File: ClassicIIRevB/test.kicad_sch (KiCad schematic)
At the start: 93 parts

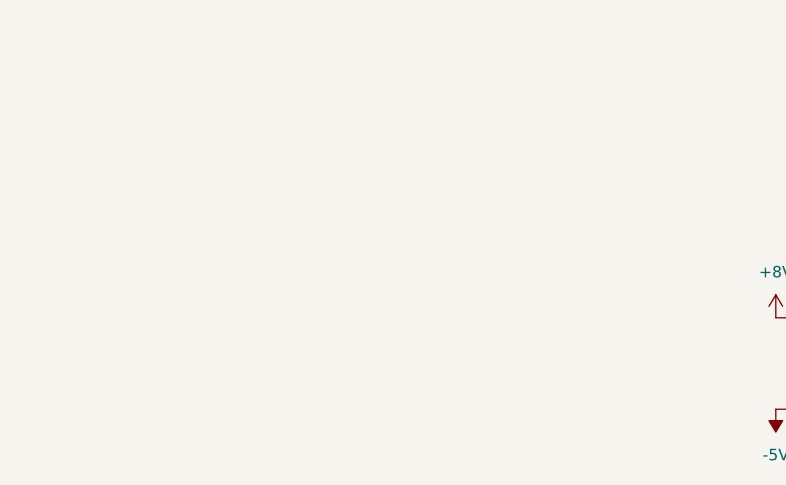
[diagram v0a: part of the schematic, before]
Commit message: Show smaller ROM footprints
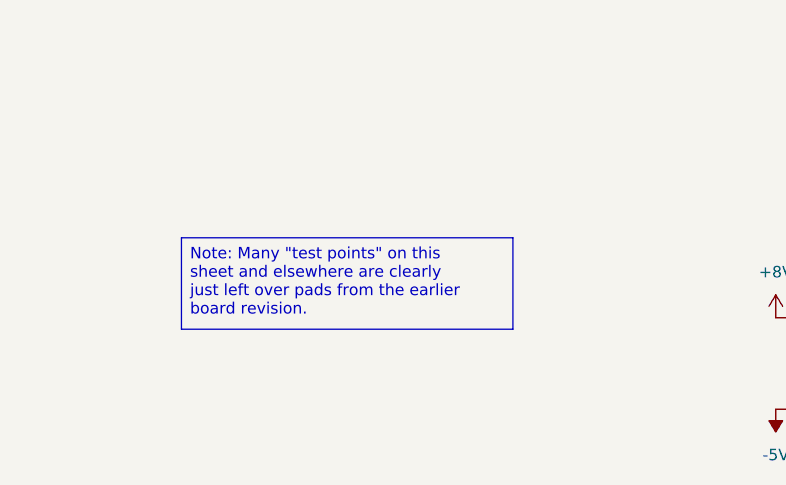
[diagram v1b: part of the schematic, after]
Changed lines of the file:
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@@
 	(title_block
 		(title "Macintosh Classic II Revision B")
-		(date "2025-05-29")
+		(date "2025-05-31")
 		(company "Apple Computer")
 		(comment 1 "drawn by Bradley Bell")
 	)
+	(text_box "Note: Many \"test points\" on this sheet and elsewhere are clearly just left over pads from the earlier board revision."
+		(exclude_from_sim no)
+		(at 48.26 171.45 0)
+		(size 36.83 10.16)
+		(margins 0.9525 0.9525 0.9525 0.9525)
+		(stroke
+			(width 0)
+			(type solid)
+		)
+		(fill
+			(type none)
+		)
+		(effects
+			(font
+				(size 1.27 1.27)
+			)
+			(justify left top)
+		)
+	)
 	(junction

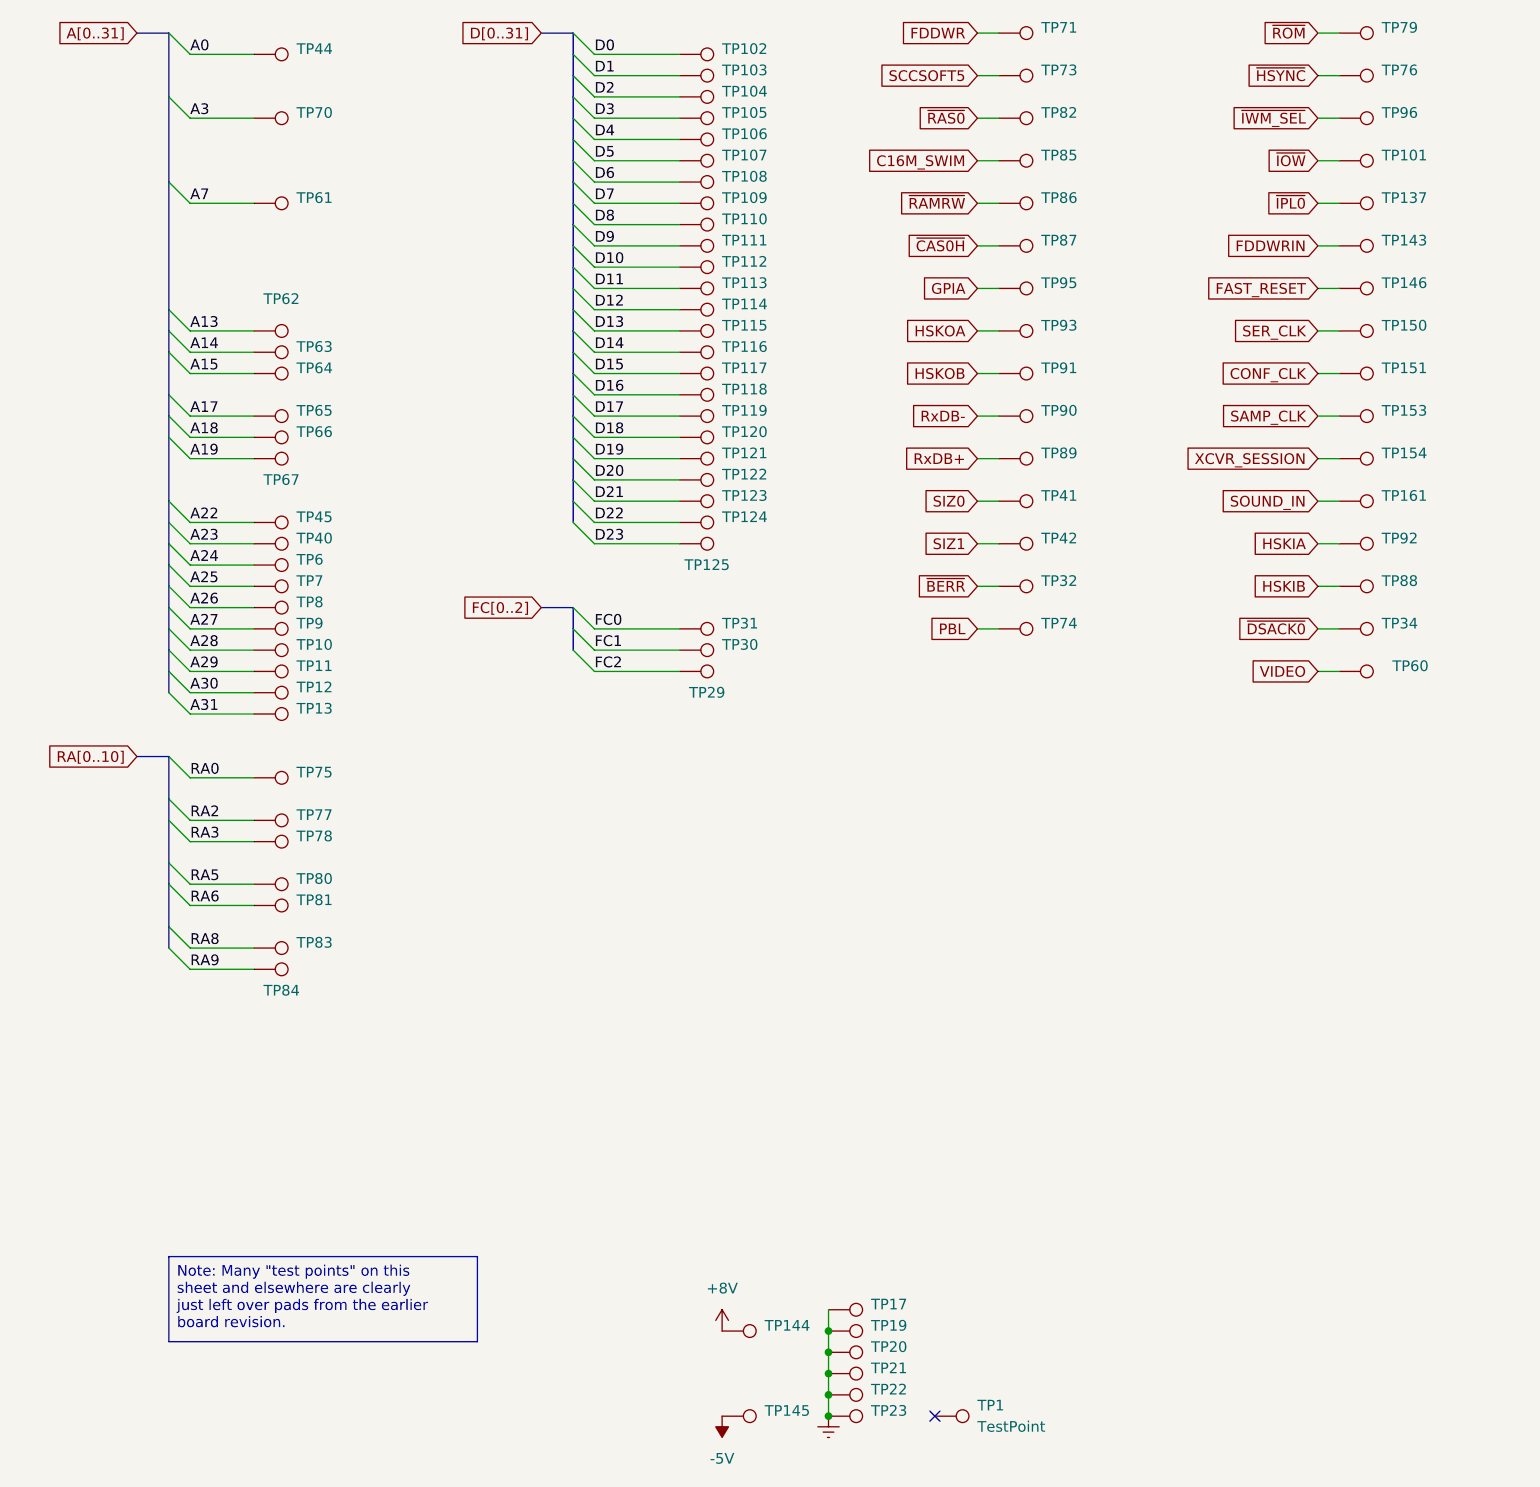
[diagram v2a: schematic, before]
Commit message: Switch to some "official" net names
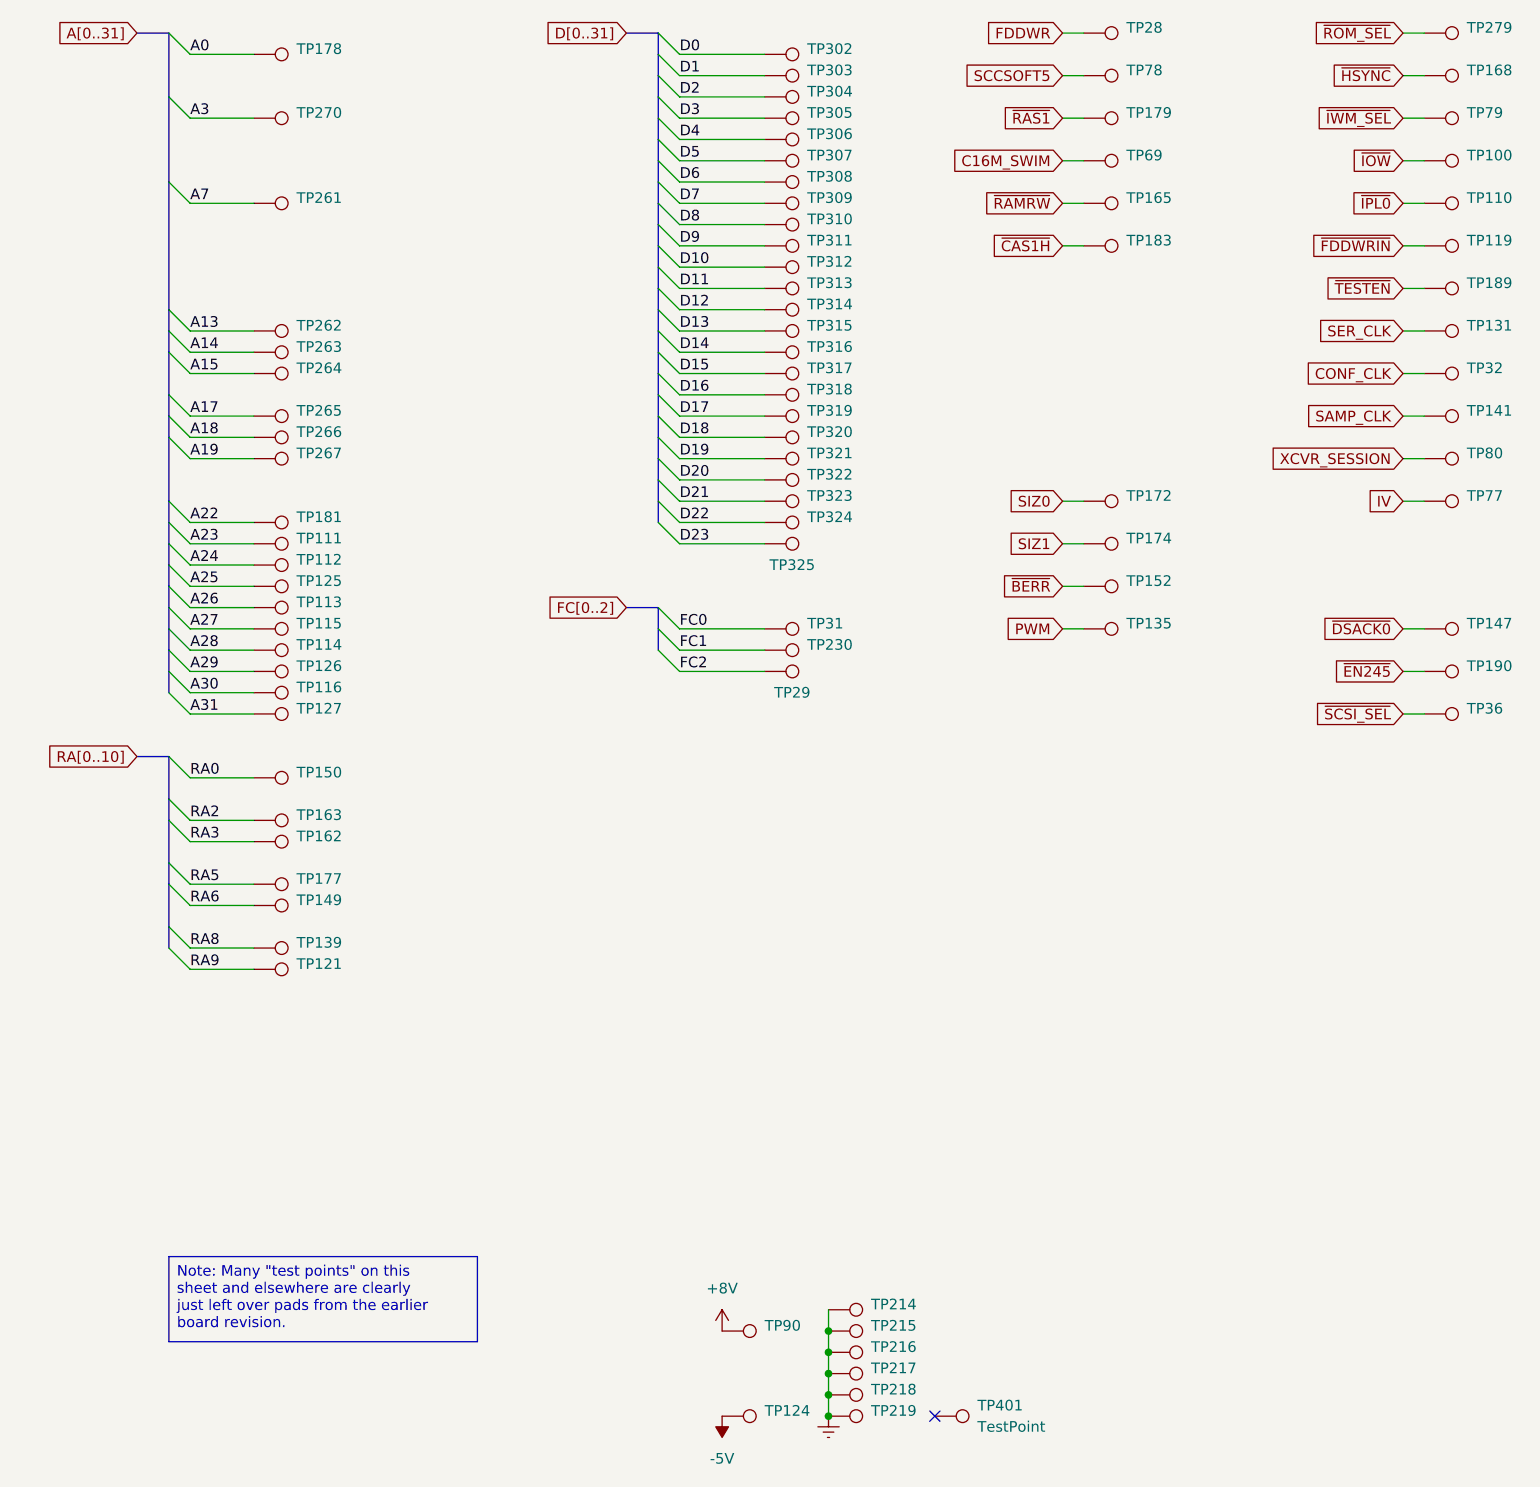
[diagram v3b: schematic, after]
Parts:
- removed TP60, TP88, TP89, TP90, TP92: ~, MyPackage:TestPoint_THTPad_D1.0mm_Drill0.5mm, symbol Connector:TestPoint
- removed TP91, TP93, TP95: ~, MyPackage:TestPoint_Pad_D1.0mm, symbol Connector:TestPoint
- added TP190, TP36: ~, MyPackage:TestPoint_THTPad_D1.0mm_Drill0.5mm, symbol Connector:TestPoint
- renumbered TP101 to TP100, TP137 to TP110, TP40 to TP111, TP6 to TP112, TP8 to TP113, TP10 to TP114, TP9 to TP115, TP12 to TP116, TP143 to TP119, TP84 to TP121, TP145 to TP124, TP7 to TP125, TP11 to TP126, TP13 to TP127, TP150 to TP131, TP74 to TP135, TP83 to TP139, TP153 to TP141, TP34 to TP147, TP81 to TP149, TP75 to TP150, TP32 to TP152, TP78 to TP162, TP77 to TP163, TP86 to TP165, TP76 to TP168, TP41 to TP172, TP42 to TP174, TP80 to TP177, TP44 to TP178, TP82 to TP179, TP45 to TP181, TP87 to TP183, TP146 to TP189, TP17 to TP214, TP19 to TP215, TP20 to TP216, TP21 to TP217, TP22 to TP218, TP23 to TP219, TP30 to TP230, TP61 to TP261, TP62 to TP262, TP63 to TP263, TP64 to TP264, TP65 to TP265, TP66 to TP266, TP67 to TP267, TP70 to TP270, TP79 to TP279, TP71 to TP28, TP102 to TP302, TP103 to TP303, TP104 to TP304, TP105 to TP305, TP106 to TP306, TP107 to TP307, TP108 to TP308, TP109 to TP309, TP110 to TP310, TP111 to TP311, TP112 to TP312, TP113 to TP313, TP114 to TP314, TP115 to TP315, TP116 to TP316, TP117 to TP317, TP118 to TP318, TP119 to TP319, TP151 to TP32, TP120 to TP320, TP121 to TP321, TP122 to TP322, TP123 to TP323, TP124 to TP324, TP125 to TP325, TP1 to TP401, TP85 to TP69, TP161 to TP77, TP73 to TP78, TP96 to TP79, TP154 to TP80, TP144 to TP90
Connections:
- net FAST_RESET renamed ~{TESTEN}
- net FDDWRIN renamed ~{FDDWRIN}
- net PBL renamed PWM
- net SOUND_IN renamed IV
- net ~{CAS0H} renamed ~{CAS1H}
- net ~{RAS0} renamed ~{RAS1}
- net ~{ROM} renamed ~{ROM_SEL}
- new net ~{EN245}: TP190.1
- new net ~{SCSI_SEL}: TP36.1
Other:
- moved on the sheet: TP100, TP110, TP119, TP131, TP135, TP141, TP147, TP152, TP165, TP168, TP172, TP174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

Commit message: update exports
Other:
- title: Macintosh Classic II Revision B -> Macintosh Classic II (Later Revision)
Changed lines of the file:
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@@
 	(paper "USLetter")
 	(title_block
-		(title "Macintosh Classic II Revision B")
-		(date "2025-06-04")
+		(title "Macintosh Classic II (Later Revision)")
+		(date "2025-06-16")
 		(company "Apple Computer")
 		(comment 1 "drawn by Bradley Bell")

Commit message: Corrections to SMDs, more improved footprints
The later revision board reproduction design is now complete.
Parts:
- TP100, TP110, TP111, TP112, TP113, TP114, TP115, TP116, TP119, TP121, TP124, TP125, TP126, TP127, TP131, TP135, TP139, TP141, TP147, TP149, TP150, TP152, TP162, TP163, TP165, TP168, TP172, TP174, TP177, TP178, TP179, TP181, TP183, TP189, TP190, TP214, TP215, TP216, TP217, TP218, TP219, TP230, TP261, TP262, TP263, TP264, TP265, TP266, TP267, TP270, TP279, TP28, TP29, TP302, TP303, TP304, TP305, TP306, TP307, TP308, TP309, TP31, TP310, TP311, TP312, TP313, TP314, TP315, TP316, TP317, TP318, TP319, TP32, TP320, TP321, TP322, TP323, TP324, TP325, TP36, TP401, TP69, TP77, TP78, TP79, TP80, TP90: now left out of the parts list
